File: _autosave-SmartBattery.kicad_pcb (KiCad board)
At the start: 2 copper layers, 100 x 70 mm, 168 parts, among them J1 USB_C_Receptacle_USB2.0, J10 JST 2P-1.0, J11 JST 2P-1.0, J2 ST-USB-003A, J3 Barrel_Jack_MountingPin, J4 JST 2P-1.0, J5 JST 2P-1.0, J6 JST 2P-1.0, J7 JST 2P-1.0, J8 JST 2P-1.0, J9 JST 2P-1.0, Q1 AO4407A, Q10 AO4468, Q11 AO4468, Q2 2n7002K, Q4 AO4468, Q6 AO4468, Q7 2n7002K, Q8 AO4468, Q9 AO4468, SW1 SW_Push, SW2 SW_Push, U1 bq2477x, U2 BQ294706DSGR, U3 ITV4030, U4 BQ40Z50, U5 LM5175PWPR

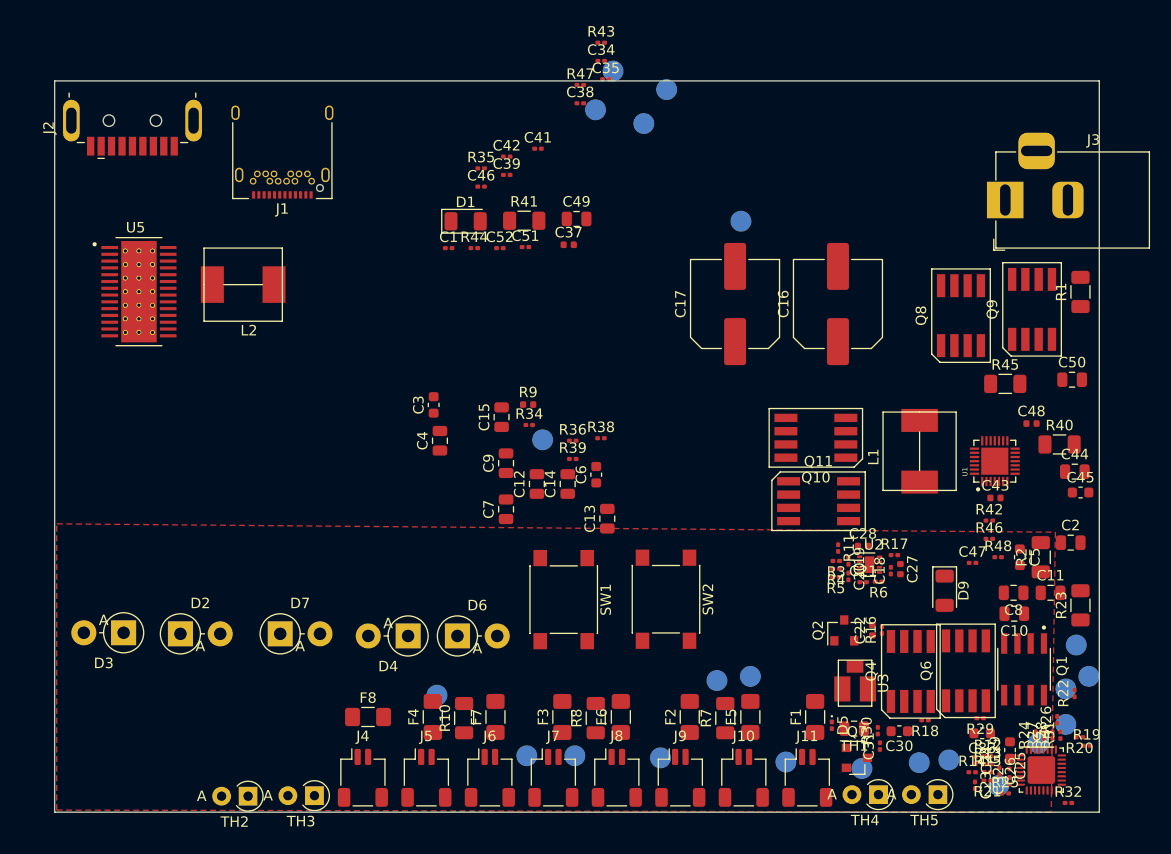
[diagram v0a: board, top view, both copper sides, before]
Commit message: Lots of changes for MFG: parts info
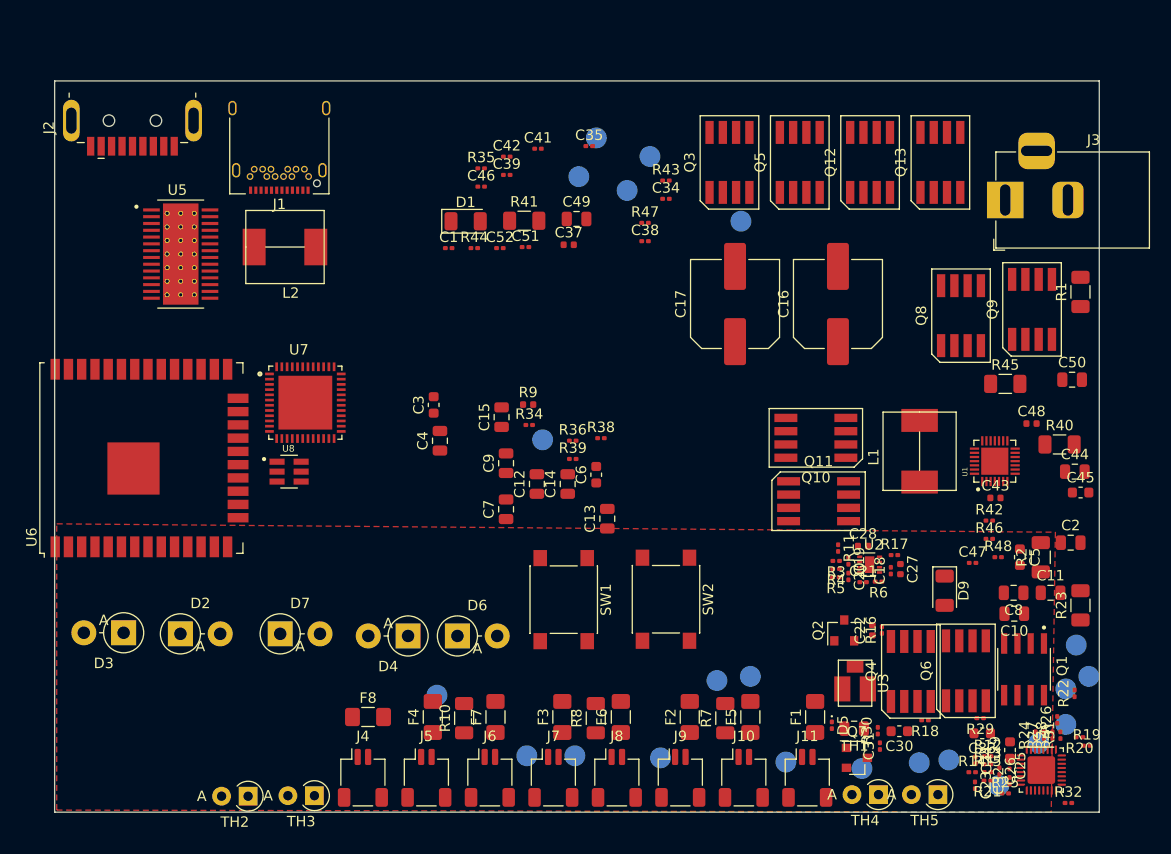
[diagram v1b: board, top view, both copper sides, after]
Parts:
- added Q12: AO4468, SmartBattery:SOIC-8_Alpha_Omega, F.Cu at (78.1, 7.80)
- added Q13: AO4468, SmartBattery:SOIC-8_Alpha_Omega, F.Cu at (84.8, 7.80)
- added Q3: AO4468, SmartBattery:SOIC-8_Alpha_Omega, F.Cu at (64.6, 7.80)
- added Q5: AO4468, SmartBattery:SOIC-8_Alpha_Omega, F.Cu at (71.3, 7.80)
- added U6: ESP32-WROOM-32U, RF_Module:ESP32-WROOM-32U, F.Cu at (8.30, 36.1)
- added U7: ATSAMD21G18A-MU, SmartBattery:QFN50P700X700X90-49N, F.Cu at (24.0, 30.8)
- added U8: TPS54202HDDCR, SmartBattery:SOT95P280X110-6N, F.Cu at (22.4, 37.4)
- moved C38 14.6 mm to (56.5, 15.3)
- moved R47 14.6 mm to (56.5, 13.6)
- moved C34 14.6 mm to (58.5, 11.3)
- moved R43 14.6 mm to (58.5, 9.54)
- moved C35 6.60 mm to (51.2, 6.24)
- moved TP20 6.60 mm to (57.0, 7.23)
- moved TP22 6.60 mm to (51.9, 5.45)
- moved TP21 6.60 mm to (54.8, 10.5)
- moved TP19 6.60 mm to (50.2, 9.16)
- moved L2 5.38 mm to (20.2, 14.0)
- moved U5 5.38 mm to (12.1, 16.6)
- moved J1 0.54 mm to (21.5, 5.44)
